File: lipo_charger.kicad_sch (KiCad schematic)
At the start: 19 parts, among them J1 USB_B_Micro, J2 22-23-2021, Q1 2N7002DW-7-F, SW1 SW_SPDT, U1 MCP73831, U2 DIO6605B, U3 AP9101CK

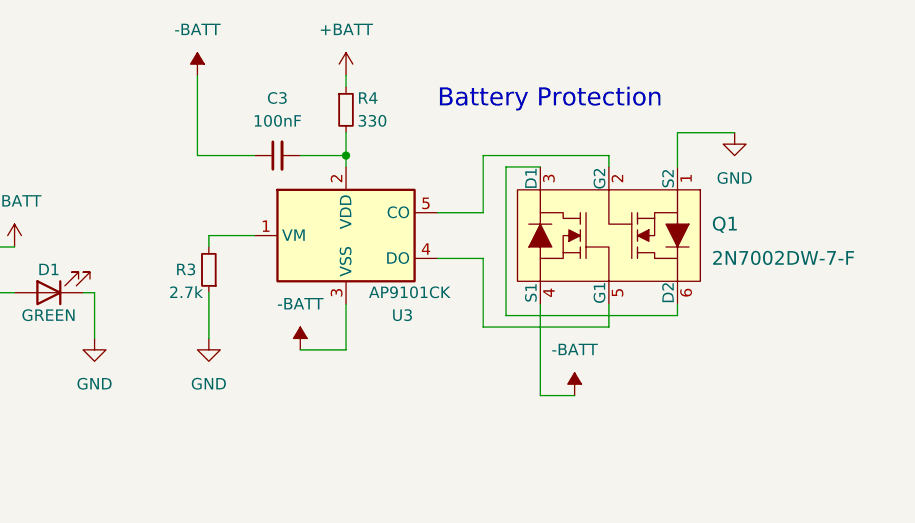
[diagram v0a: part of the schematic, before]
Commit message: Replace Q1 NMOS and fix R3 val
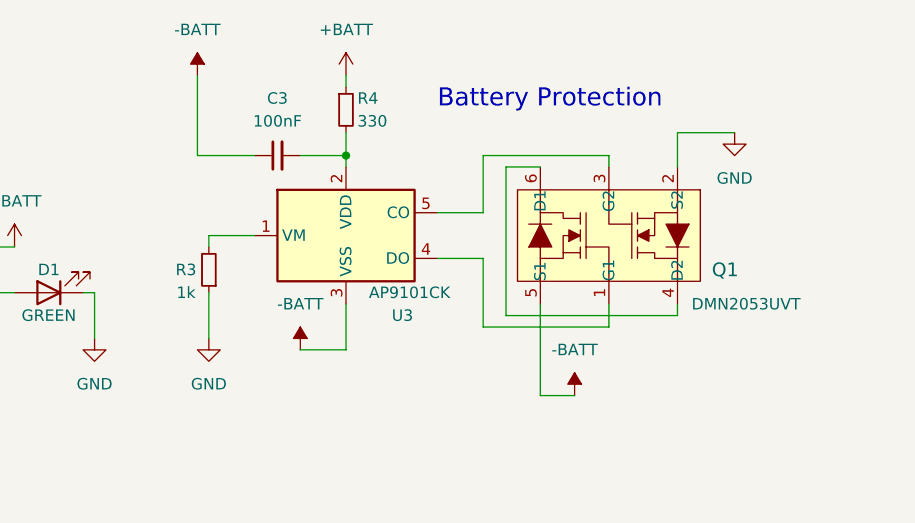
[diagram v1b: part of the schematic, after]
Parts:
- Q1: value 2N7002DW-7-F -> DMN2053UVT; footprint digikey-footprints:SOT-363 -> Package_TO_SOT_SMD:TSOT-23-6; symbol dk_Transistors-FETs-MOSFETs-Arrays:2N7002DW-7-F -> DMN2053UVT:DMN2053UVT; Category Discrete Semiconductor Products -> (none); DK_Datasheet_Link https://www.diodes.com/assets/Datasheets/ds30120.pdf -> (none); DK_Detail_Page /product-detail/en/diodes-incorporated/2N7002DW-7-F/2N7002D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 -> (none); Digi-Key_PN 2N7002DW-FDICT-ND -> (none); Family Transistors - FETs, MOSFETs - Arrays -> (none); MPN 2N7002DW-7-F -> (none); Manufacturer Diodes Incorporated -> (none); Status Active -> (none)
- R3: value 2.7k -> 1k
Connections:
- net -BATT: now also Q1.5 (S1); no longer Q1.4 (S1)
- net GND: now also Q1.2 (S2); no longer Q1.1 (S2)
- net at U3.5 (CO): now also Q1.3 (G2); no longer Q1.2 (G2)
- net at Q1.6 (D1): now also Q1.4 (D2); no longer Q1.3 (D1)
- net at U3.4 (DO): now also Q1.1 (G1); no longer Q1.5 (G1)
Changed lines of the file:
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@@
     (pin "1")
   )
-  (symbol (lib_id "dk_Transistors-FETs-MOSFETs-Arrays:2N7002DW-7-F") (at 167.64 76.2 270) (unit 1)
-    (in_bom yes) (on_board yes) (fields_autoplaced)
-    (property "Reference" "Q1" (id 0) (at 176.53 74.93 90)
+  (symbol (lib_id "DMN2053UVT:DMN2053UVT") (at 165.1 76.2 270) (unit 1)
+    (in_bom yes) (on_board yes)
+    (property "Reference" "Q1" (id 0) (at 176.53 80.01 90)
       (effects (font (size 1.524 1.524)) (justify left))
     )
-    (property "Value" "2N7002DW-7-F" (id 1) (at 176.53 78.74 90)
-      (effects (font (size 1.524 1.524)) (justify left))
-    )
-    (property "Footprint" "digikey-footprints:SOT-363" (id 2) (at 172.72 81.28 0)
-      (effects (font (size 1.524 1.524)) (justify left) hide)
-    )
-    (property "Datasheet" "https://www.diodes.com/assets/Datasheets/ds30120.pdf" (id 3) (at 175.26 81.28 0)
-      (effects (font (size 1.524 1.524)) (justify left) hide)
-    )
-    (property "Digi-Key_PN" "2N7002DW-FDICT-ND" (id 4) (at 177.8 81.28 0)
-      (effects (font (size 1.524 1.524)) (justify left) hide)
-    )
-    (property "MPN" "2N7002DW-7-F" (id 5) (at 180.34 81.28 0)
-      (effects (font (size 1.524 1.524)) (justify left) hide)
-    )
-    (property "Category" "Discrete Semiconductor Products" (id 6) (at 182.88 81.28 0)
-      (effects (font (size 1.524 1.524)) (justify left) hide)
-    )
-    (property "Family" "Transistors - FETs, MOSFETs - Arrays" (id 7) (at 185.42 81.28 0)
-      (effects (font (size 1.524 1.524)) (justify left) hide)
-    )
-    (property "DK_Datasheet_Link" "https://www.diodes.com/assets/Datasheets/ds30120.pdf" (id 8) (at 187.96 81.28 0)
-      (effects (font (size 1.524 1.524)) (justify left) hide)
-    )
-    (property "DK_Detail_Page" "/product-detail/en/diodes-incorporated/2N7002DW-7-F/2N7002DW-FDICT-ND/750003" (id 9) (at 190.5 81.28 0)
-      (effects (font (size 1.524 1.524)) (justify left) hide)
-    )
-    (property "Description" "MOSFET 2N-CH 60V 0.23A SOT-363" (id 10) (at 193.04 81.28 0)
-      (effects (font (size 1.524 1.524)) (justify left) hide)
-    )
-    (property "Manufacturer" "Diodes Incorporated" (id 11) (at 195.58 81.28 0)
-      (effects (font (size 1.524 1.524)) (justify left) hide)
-    )
-    (property "Status" "Active" (id 12) (at 198.12 81.28 0)
-      (effects (font (size 1.524 1.524)) (justify left) hide)
+    (property "Value" "DMN2053UVT" (id 1) (at 180.34 83.82 90))
+    (property "Footprint" "Package_TO_SOT_SMD:TSOT-23-6" (id 2) (at 144.78 82.55 0)
+      (effects (font (size 1.27 1.27)) hide)
+    )
+    (property "Datasheet" "https://www.mouser.com/datasheet/2/115/DIOD_S_A0006646726_1-2542802.pdf" (id 3) (at 148.59 87.63 0)
+      (effects (font (size 1.27 1.27)) hide)
     )
     (pin "1")
@@
     (in_bom yes) (on_board yes)
     (property "Reference" "R3" (id 0) (at 118.11 80.01 0))
-    (property "Value" "2.7k" (id 1) (at 118.11 82.55 0))
+    (property "Value" "1k" (id 1) (at 118.11 82.55 0))
     (property "Footprint" "Resistor_SMD:R_0805_2012Metric_Pad1.20x1.40mm_HandSolder" (id 2) (at 120.65 80.01 0)
       (effects (font (size 1.27 1.27)) hide)
@@
     )
     (path "/47eedd86-7c83-4329-b0bc-ff9bbee686e9"
-      (reference "Q1") (unit 1) (value "2N7002DW-7-F") (footprint "digikey-footprints:SOT-363")
+      (reference "Q1") (unit 1) (value "DMN2053UVT") (footprint "Package_TO_SOT_SMD:TSOT-23-6")
     )
     (path "/e812583b-046a-424b-b642-5fa655270f02"
@@
     )
     (path "/56e6188e-bbbc-4aaa-8e4c-89a99b5f65d8"
-      (reference "R3") (unit 1) (value "2.7k") (footprint "Resistor_SMD:R_0805_2012Metric_Pad1.20x1.40mm_HandSolder")
+      (reference "R3") (unit 1) (value "1k") (footprint "Resistor_SMD:R_0805_2012Metric_Pad1.20x1.40mm_HandSolder")
     )
     (path "/c2292aaf-d708-456d-8b2c-7fe6a17b8c3e"

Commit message: Replace switch and reroute
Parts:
- SW1: footprint Button_Switch_THT:SW_Slide_1P2T_CK_OS102011MS2Q -> footprint_libs:SW_EG1224
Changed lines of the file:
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@@
     (property "Reference" "SW1" (id 0) (at 62.23 111.76 0))
     (property "Value" "SW_SPDT" (id 1) (at 62.23 114.3 0))
-    (property "Footprint" "Button_Switch_THT:SW_Slide_1P2T_CK_OS102011MS2Q" (id 2) (at 60.96 118.11 0)
+    (property "Footprint" "footprint_libs:SW_EG1224" (id 2) (at 60.96 118.11 0)
       (effects (font (size 1.27 1.27)) hide)
     )
@@
     )
     (path "/2886b9cb-f705-411b-b7c5-ebafca1f4a4a"
-      (reference "SW1") (unit 1) (value "SW_SPDT") (footprint "Button_Switch_THT:SW_Slide_1P2T_CK_OS102011MS2Q")
+      (reference "SW1") (unit 1) (value "SW_SPDT") (footprint "footprint_libs:SW_EG1224")
     )
     (path "/30f62251-7f9a-407f-abad-8308def083a6"

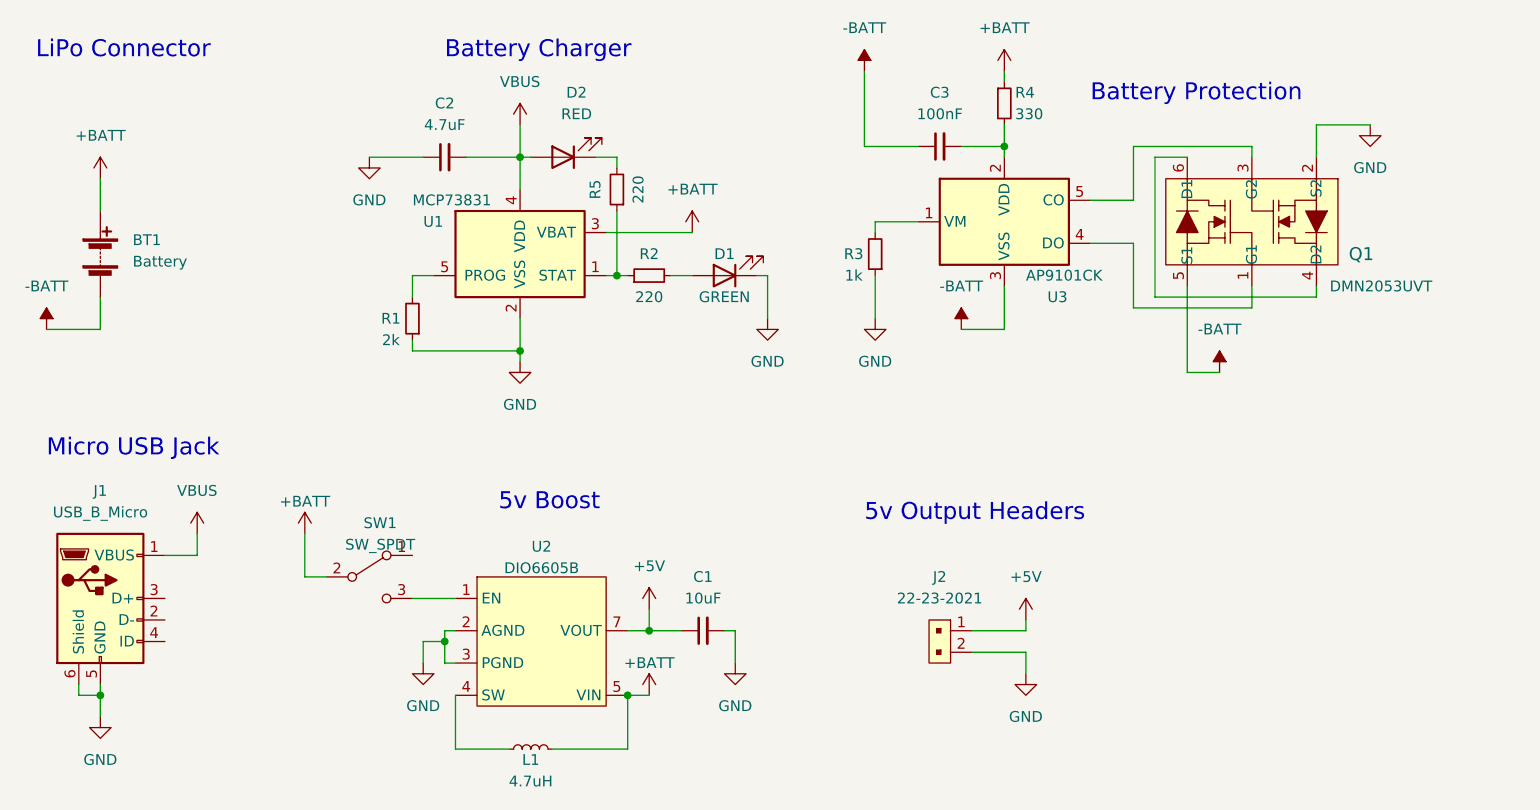
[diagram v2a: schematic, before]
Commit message: Replace switch and rewire schematic
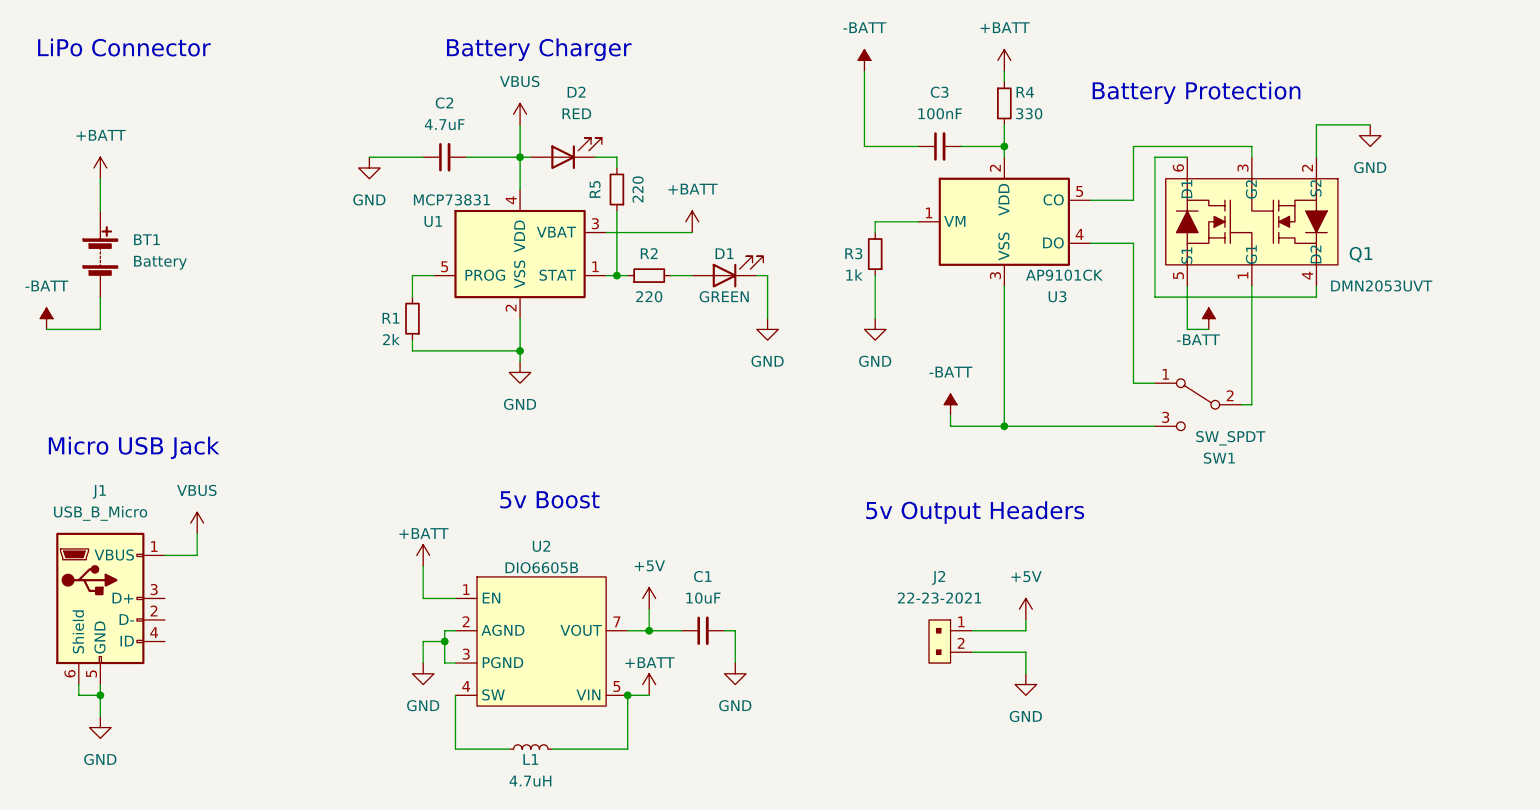
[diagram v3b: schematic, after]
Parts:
- SW1: footprint footprint_libs:SW_EG1224 -> Button_Switch_THT:SW_CuK_OS102011MA1QN1_SPDT_Angled
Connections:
- net +BATT: now also U2.1 (EN); no longer SW1.2 (B)
- net -BATT: now also SW1.3 (C)
- net at SW1.1 (A): now also U3.4 (DO)
- net at Q1.1 (G1): now also SW1.2 (B); no longer U3.4 (DO)
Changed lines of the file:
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@@
   (junction (at 78.74 91.44) (diameter 0) (color 0 0 0 0)
   )
+  (junction (at 135.89 100.33) (diameter 0) (color 0 0 0 0)
+  )
   (junction (at 90.17 82.55) (diameter 0) (color 0 0 0 0)
   )
@@
   (junction (at 91.44 132.08) (diameter 0) (color 0 0 0 0)
   )
-  (wire (pts (xy 151.13 78.74) (xy 151.13 86.36))
+  (wire (pts (xy 151.13 78.74) (xy 151.13 95.25))
     (stroke (width 0) (type default) (color 0 0 0 0))
   )
@@
     (stroke (width 0) (type default) (color 0 0 0 0))
   )
-  (wire (pts (xy 135.89 88.9) (xy 130.81 88.9))
-    (stroke (width 0) (type default) (color 0 0 0 0))
-  )
   (wire (pts (xy 68.58 82.55) (xy 66.04 82.55))
     (stroke (width 0) (type default) (color 0 0 0 0))
@@
     (stroke (width 0) (type default) (color 0 0 0 0))
   )
+  (wire (pts (xy 153.67 85.09) (xy 172.72 85.09))
+    (stroke (width 0) (type default) (color 0 0 0 0))
+  )
   (wire (pts (xy 93.98 124.46) (xy 93.98 121.92))
     (stroke (width 0) (type default) (color 0 0 0 0))
@@
     (stroke (width 0) (type default) (color 0 0 0 0))
   )
-  (wire (pts (xy 53.34 118.11) (xy 55.88 118.11))
-    (stroke (width 0) (type default) (color 0 0 0 0))
-  )
   (wire (pts (xy 119.38 58.42) (xy 119.38 67.31))
     (stroke (width 0) (type default) (color 0 0 0 0))
@@
     (stroke (width 0) (type default) (color 0 0 0 0))
   )
-  (wire (pts (xy 165.1 86.36) (xy 165.1 83.82))
-    (stroke (width 0) (type default) (color 0 0 0 0))
-  )
-  (wire (pts (xy 151.13 86.36) (xy 165.1 86.36))
+  (wire (pts (xy 165.1 83.82) (xy 165.1 97.79))
     (stroke (width 0) (type default) (color 0 0 0 0))
   )
@@
     (stroke (width 0) (type default) (color 0 0 0 0))
   )
-  (wire (pts (xy 53.34 113.03) (xy 53.34 118.11))
+  (wire (pts (xy 67.31 120.65) (xy 67.31 116.84))
     (stroke (width 0) (type default) (color 0 0 0 0))
   )
@@
     (stroke (width 0) (type default) (color 0 0 0 0))
   )
+  (wire (pts (xy 135.89 100.33) (xy 135.89 83.82))
+    (stroke (width 0) (type default) (color 0 0 0 0))
+  )
   (wire (pts (xy 172.72 64.77) (xy 179.07 64.77))
     (stroke (width 0) (type default) (color 0 0 0 0))
@@
     (stroke (width 0) (type default) (color 0 0 0 0))
   )
+  (wire (pts (xy 129.54 99.06) (xy 129.54 100.33))
+    (stroke (width 0) (type default) (color 0 0 0 0))
+  )
   (wire (pts (xy 71.12 132.08) (xy 71.12 138.43))
     (stroke (width 0) (type default) (color 0 0 0 0))
@@
     (stroke (width 0) (type default) (color 0 0 0 0))
   )
+  (wire (pts (xy 165.1 97.79) (xy 163.83 97.79))
+    (stroke (width 0) (type default) (color 0 0 0 0))
+  )
   (wire (pts (xy 130.81 67.31) (xy 135.89 67.31))
     (stroke (width 0) (type default) (color 0 0 0 0))
   )
+  (wire (pts (xy 153.67 100.33) (xy 135.89 100.33))
+    (stroke (width 0) (type default) (color 0 0 0 0))
+  )
   (wire (pts (xy 40.64 115.57) (xy 40.64 113.03))
     (stroke (width 0) (type default) (color 0 0 0 0))
@@
     (stroke (width 0) (type default) (color 0 0 0 0))
   )
-  (wire (pts (xy 157.48 83.82) (xy 157.48 93.98))
-    (stroke (width 0) (type default) (color 0 0 0 0))
-  )
-  (wire (pts (xy 135.89 83.82) (xy 135.89 88.9))
+  (wire (pts (xy 157.48 83.82) (xy 157.48 88.9))
+    (stroke (width 0) (type default) (color 0 0 0 0))
+  )
+  (wire (pts (xy 151.13 95.25) (xy 153.67 95.25))
     (stroke (width 0) (type default) (color 0 0 0 0))
   )
@@
     (stroke (width 0) (type default) (color 0 0 0 0))
   )
-  (wire (pts (xy 66.04 120.65) (xy 71.12 120.65))
-    (stroke (width 0) (type default) (color 0 0 0 0))
-  )
   (wire (pts (xy 132.08 124.46) (xy 138.43 124.46))
     (stroke (width 0) (type default) (color 0 0 0 0))
   )
+  (wire (pts (xy 129.54 100.33) (xy 135.89 100.33))
+    (stroke (width 0) (type default) (color 0 0 0 0))
+  )
   (wire (pts (xy 132.08 127) (xy 138.43 127))
     (stroke (width 0) (type default) (color 0 0 0 0))
   )
+  (wire (pts (xy 71.12 120.65) (xy 67.31 120.65))
+    (stroke (width 0) (type default) (color 0 0 0 0))
+  )
   (wire (pts (xy 120.65 76.2) (xy 120.65 77.47))
     (stroke (width 0) (type default) (color 0 0 0 0))
@@
     (stroke (width 0) (type default) (color 0 0 0 0))
   )
-  (wire (pts (xy 153.67 85.09) (xy 172.72 85.09))
-    (stroke (width 0) (type default) (color 0 0 0 0))
-  )
   (wire (pts (xy 78.74 68.58) (xy 78.74 72.39))
     (stroke (width 0) (type default) (color 0 0 0 0))
@@
     (stroke (width 0) (type default) (color 0 0 0 0))
   )
-  (wire (pts (xy 157.48 93.98) (xy 161.29 93.98))
+  (wire (pts (xy 157.48 88.9) (xy 160.02 88.9))
     (stroke (width 0) (type default) (color 0 0 0 0))
   )
@@
     (pin "1")
   )
-  (symbol (lib_id "power:-BATT") (at 161.29 93.98 0) (unit 1)
-    (in_bom yes) (on_board yes) (fields_autoplaced)
-    (property "Reference" "#PWR017" (id 0) (at 161.29 97.79 0)
-      (effects (font (size 1.27 1.27)) hide)
-    )
-    (property "Value" "-BATT" (id 1) (at 161.29 88.9 0))
-    (property "Footprint" "" (id 2) (at 161.29 93.98 0)
-      (effects (font (size 1.27 1.27)) hide)
-    )
-    (property "Datasheet" "" (id 3) (at 161.29 93.98 0)
+  (symbol (lib_id "power:-BATT") (at 160.02 88.9 0) (unit 1)
+    (in_bom yes) (on_board yes)
+    (property "Reference" "#PWR017" (id 0) (at 160.02 92.71 0)
+      (effects (font (size 1.27 1.27)) hide)
+    )
+    (property "Value" "-BATT" (id 1) (at 158.75 90.17 0))
+    (property "Footprint" "" (id 2) (at 160.02 88.9 0)
+      (effects (font (size 1.27 1.27)) hide)
+    )
+    (property "Datasheet" "" (id 3) (at 160.02 88.9 0)
       (effects (font (size 1.27 1.27)) hide)
     )
@@
     (pin "6")
   )
-  (symbol (lib_id "Switch:SW_SPDT") (at 60.96 118.11 0) (unit 1)
-    (in_bom yes) (on_board yes)
-    (property "Reference" "SW1" (id 0) (at 62.23 111.76 0))
-    (property "Value" "SW_SPDT" (id 1) (at 62.23 114.3 0))
-    (property "Footprint" "footprint_libs:SW_EG1224" (id 2) (at 60.96 118.11 0)
-      (effects (font (size 1.27 1.27)) hide)
-    )
-    (property "Datasheet" "~" (id 3) (at 60.96 118.11 0)
-      (effects (font (size 1.27 1.27)) hide)
-    )
-    (pin "1")
-    (pin "2")
-    (pin "3")
-  )
-  (symbol (lib_id "power:+BATT") (at 53.34 113.03 0) (unit 1)
-    (in_bom yes) (on_board yes)
-    (property "Reference" "#PWR07" (id 0) (at 53.34 116.84 0)
-      (effects (font (size 1.27 1.27)) hide)
-    )
-    (property "Value" "+BATT" (id 1) (at 53.34 109.22 0))
-    (property "Footprint" "" (id 2) (at 53.34 113.03 0)
-      (effects (font (size 1.27 1.27)) hide)
-    )
-    (property "Datasheet" "" (id 3) (at 53.34 113.03 0)
+  (symbol (lib_id "power:+BATT") (at 67.31 116.84 0) (unit 1)
+    (in_bom yes) (on_board yes)
+    (property "Reference" "#PWR07" (id 0) (at 67.31 120.65 0)
+      (effects (font (size 1.27 1.27)) hide)
+    )
+    (property "Value" "+BATT" (id 1) (at 67.31 113.03 0))
+    (property "Footprint" "" (id 2) (at 67.31 116.84 0)
+      (effects (font (size 1.27 1.27)) hide)
+    )
+    (property "Datasheet" "" (id 3) (at 67.31 116.84 0)
       (effects (font (size 1.27 1.27)) hide)
     )
@@
     (pin "2")
   )
+  (symbol (lib_id "power:-BATT") (at 129.54 99.06 0) (unit 1)
+    (in_bom yes) (on_board yes)
+    (property "Reference" "#PWR0103" (id 0) (at 129.54 102.87 0)
+      (effects (font (size 1.27 1.27)) hide)
+    )
+    (property "Value" "-BATT" (id 1) (at 129.54 93.98 0))
+    (property "Footprint" "" (id 2) (at 129.54 99.06 0)
+      (effects (font (size 1.27 1.27)) hide)
+    )
+    (property "Datasheet" "" (id 3) (at 129.54 99.06 0)
+      (effects (font (size 1.27 1.27)) hide)
+    )
+    (pin "1")
+  )
   (symbol (lib_id "power:GND") (at 138.43 129.54 0) (unit 1)
     (in_bom yes) (on_board yes) (fields_autoplaced)
@@
     (pin "2")
   )
-  (symbol (lib_id "power:-BATT") (at 130.81 88.9 0) (unit 1)
-    (in_bom yes) (on_board yes) (fields_autoplaced)
-    (property "Reference" "#PWR015" (id 0) (at 130.81 92.71 0)
-      (effects (font (size 1.27 1.27)) hide)
-    )
-    (property "Value" "-BATT" (id 1) (at 130.81 83.82 0))
-    (property "Footprint" "" (id 2) (at 130.81 88.9 0)
-      (effects (font (size 1.27 1.27)) hide)
-    )
-    (property "Datasheet" "" (id 3) (at 130.81 88.9 0)
-      (effects (font (size 1.27 1.27)) hide)
-    )
-    (pin "1")
+  (symbol (lib_id "Switch:SW_SPDT") (at 158.75 97.79 0) (mirror y) (unit 1)
+    (in_bom yes) (on_board yes)
+    (property "Reference" "SW1" (id 0) (at 161.29 104.14 0))
+    (property "Value" "SW_SPDT" (id 1) (at 162.56 101.6 0))
+    (property "Footprint" "Button_Switch_THT:SW_CuK_OS102011MA1QN1_SPDT_Angled" (id 2) (at 158.75 97.79 0)
+      (effects (font (size 1.27 1.27)) hide)
+    )
+    (property "Datasheet" "~" (id 3) (at 158.75 97.79 0)
+      (effects (font (size 1.27 1.27)) hide)
+    )
+    (pin "1")
+    (pin "2")
+    (pin "3")
   )
   (sheet_instances
@@
       (reference "#PWR014") (unit 1) (value "GND") (footprint "")
     )
-    (path "/fe5914db-239a-4e81-95d1-2269d296fc5c"
-      (reference "#PWR015") (unit 1) (value "-BATT") (footprint "")
-    )
     (path "/89bacdac-ded2-4289-992b-bcff7d61c010"
       (reference "#PWR016") (unit 1) (value "+BATT") (footprint "")
@@
       (reference "#PWR0102") (unit 1) (value "VBUS") (footprint "")
     )
+    (path "/c7a25488-fce2-43a4-8708-c55f5b10352b"
+      (reference "#PWR0103") (unit 1) (value "-BATT") (footprint "")
+    )
     (path "/686758ed-33a5-4b43-b0f3-d9e0a9b96ca5"
       (reference "BT1") (unit 1) (value "Battery") (footprint "Connector_JST:JST_PH_B2B-PH-SM4-TB_1x02-1MP_P2.00mm_Vertical")
@@
       (reference "R5") (unit 1) (value "220") (footprint "Resistor_SMD:R_0805_2012Metric_Pad1.20x1.40mm_HandSolder")
     )
-    (path "/2886b9cb-f705-411b-b7c5-ebafca1f4a4a"
-      (reference "SW1") (unit 1) (value "SW_SPDT") (footprint "footprint_libs:SW_EG1224")
+    (path "/fa0c82d3-c792-441f-8df6-1d0b0aa9dbe3"
+      (reference "SW1") (unit 1) (value "SW_SPDT") (footprint "Button_Switch_THT:SW_CuK_OS102011MA1QN1_SPDT_Angled")
     )
     (path "/30f62251-7f9a-407f-abad-8308def083a6"
